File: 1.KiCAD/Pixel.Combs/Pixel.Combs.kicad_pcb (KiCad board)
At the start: 2 copper layers, 247 x 80 mm, 85 parts

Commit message: Updated Combs
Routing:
- net (no net): track 0.00 -> 328.9 mm, vias 57 -> 100

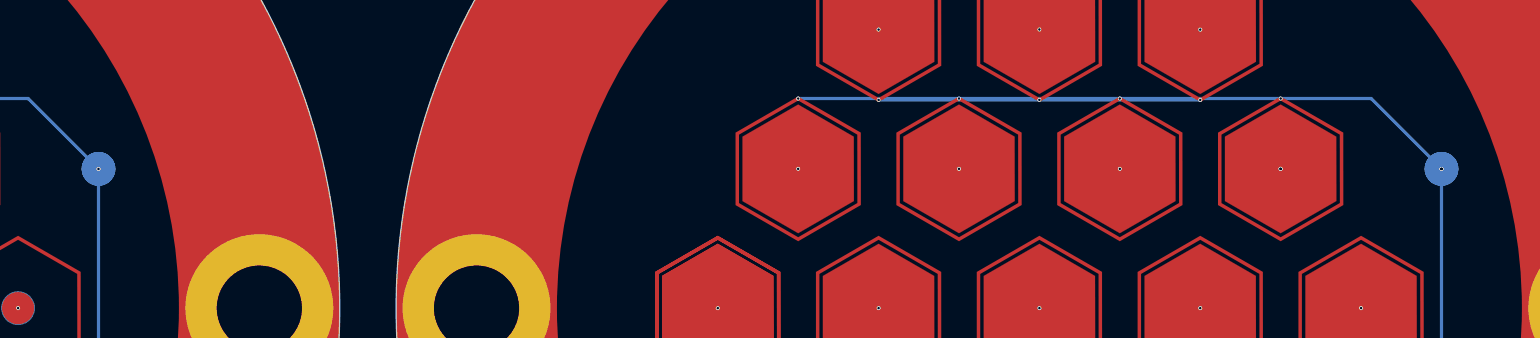
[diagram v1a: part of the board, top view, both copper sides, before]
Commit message: Spaced collection board traces
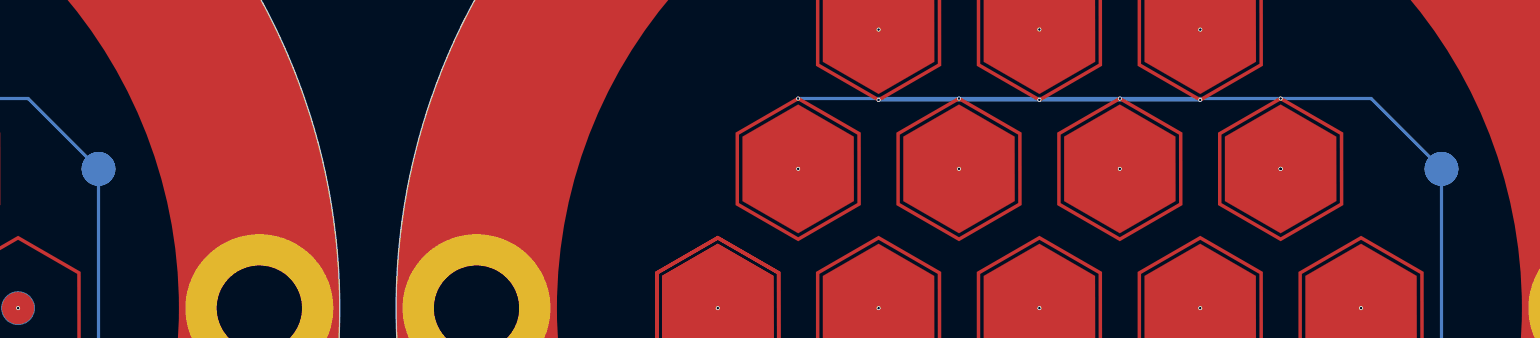
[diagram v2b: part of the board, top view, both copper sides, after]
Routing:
- net (no net): vias 100 -> 97
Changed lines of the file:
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@@
   (via blind (at 247.290237 56.129937) (size 0.25) (drill 0.15) (layers "F.Cu" "B.Cu") (net 0))
   (via blind (at 133.785 56.13) (size 0.25) (drill 0.15) (layers "F.Cu" "B.Cu") (net 0))
-  (via blind (at 257.290237 56.129937) (size 0.25) (drill 0.15) (layers "F.Cu" "B.Cu") (net 0))
   (via blind (at 138.785 82.11) (size 0.25) (drill 0.15) (layers "F.Cu" "B.Cu") (net 0))
   (via blind (at 158.785 77.735) (size 0.25) (drill 0.15) (layers "F.Cu" "B.Cu") (net 0))
@@
   (via blind (at 237.290237 56.129937) (size 0.25) (drill 0.15) (layers "F.Cu" "B.Cu") (net 0))
   (via blind (at 222.289859 64.790093) (size 0.25) (drill 0.15) (layers "F.Cu" "B.Cu") (net 0))
-  (via blind (at 173.785 56.13) (size 0.25) (drill 0.15) (layers "F.Cu" "B.Cu") (net 0))
   (via blind (at 138.785 69.165) (size 0.25) (drill 0.15) (layers "F.Cu" "B.Cu") (net 0))
   (via blind (at 60.280237 73.449937) (size 0.25) (drill 0.15) (layers "F.Cu" "B.Cu") (net 0))
@@
   (via blind (at 247.290237 69.074937) (size 0.25) (drill 0.15) (layers "F.Cu" "B.Cu") (net 0))
   (via blind (at 75.280237 64.789937) (size 0.25) (drill 0.15) (layers "F.Cu" "B.Cu") (net 0))
-  (via blind (at 257.290237 56.129937) (size 0.25) (drill 0.15) (layers "F.Cu" "B.Cu") (net 0))
   (via blind (at 153.785 73.45) (size 0.25) (drill 0.15) (layers "F.Cu" "B.Cu") (net 0))
   (via blind (at 50.280237 56.129937) (size 0.25) (drill 0.15) (layers "F.Cu" "B.Cu") (net 0))

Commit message: Thickened ground traces and updated channel wires
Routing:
- net (no net): track 328.9 -> 268.9 mm
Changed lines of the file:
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@@
   (via blind (at 217.289859 56.130093) (size 0.25) (drill 0.15) (layers "F.Cu" "B.Cu") (net 0))
   (via blind (at 70.280237 56.129937) (size 0.25) (drill 0.15) (layers "F.Cu" "B.Cu") (net 0))
-  (segment (start 169.41 51.755) (end 173.785 56.13) (width 0.2) (layer "B.Cu") (net 0))
+  (segment (start 169.41 51.755) (end 173.785 56.13) (width 1) (layer "B.Cu") (net 0))
   (segment (start 222.289859 51.845093) (end 242.290081 51.845093) (width 0.2) (layer "B.Cu") (net 0))
-  (segment (start 252.915237 51.754937) (end 257.290237 56.129937) (width 0.2) (layer "B.Cu") (net 0))
-  (segment (start 217.290237 69.074937) (end 247.290237 69.074937) (width 0.2) (layer "B.Cu") (net 0))
-  (segment (start 222.289859 69.165093) (end 222.289859 77.735093) (width 0.2) (layer "B.Cu") (net 0))
-  (segment (start 128.785 69.165) (end 168.785 69.165) (width 0.2) (layer "B.Cu") (net 0))
-  (segment (start 255.469907 69.165093) (end 252.289859 69.165093) (width 0.2) (layer "B.Cu") (net 0))
+  (segment (start 252.915237 51.754937) (end 257.290237 56.129937) (width 1) (layer "B.Cu") (net 0))
+  (segment (start 222.289859 69.165093) (end 222.289859 77.735093) (width 1) (layer "B.Cu") (net 0))
+  (segment (start 128.785 69.165) (end 168.785 69.165) (width 1) (layer "B.Cu") (net 0))
+  (segment (start 255.469907 69.165093) (end 252.289859 69.165093) (width 1) (layer "B.Cu") (net 0))
   (segment (start 242.290081 51.845093) (end 242.290237 51.844937) (width 0.2) (layer "B.Cu") (net 0))
-  (segment (start 257.290237 67.344763) (end 255.469907 69.165093) (width 0.2) (layer "B.Cu") (net 0))
-  (segment (start 173.785 56.13) (end 173.785 67.225) (width 0.2) (layer "B.Cu") (net 0))
-  (segment (start 217.289859 51.755093) (end 247.290081 51.755093) (width 0.2) (layer "B.Cu") (net 0))
-  (segment (start 133.785 51.755) (end 163.785 51.755) (width 0.2) (layer "B.Cu") (net 0))
-  (segment (start 247.290237 51.754937) (end 252.915237 51.754937) (width 0.2) (layer "B.Cu") (net 0))
-  (segment (start 133.785 69.075) (end 163.785 69.075) (width 0.2) (layer "B.Cu") (net 0))
-  (segment (start 158.785 77.735) (end 158.785 69.165) (width 0.2) (layer "B.Cu") (net 0))
-  (segment (start 212.289859 69.165093) (end 252.289859 69.165093) (width 0.2) (layer "B.Cu") (net 0))
-  (segment (start 242.289859 69.165093) (end 242.289859 77.735093) (width 0.2) (layer "B.Cu") (net 0))
-  (segment (start 148.785 77.735) (end 148.785 69.165) (width 0.2) (layer "B.Cu") (net 0))
-  (segment (start 173.785 67.225) (end 171.845 69.165) (width 0.2) (layer "B.Cu") (net 0))
-  (segment (start 163.785 51.755) (end 169.41 51.755) (width 0.2) (layer "B.Cu") (net 0))
+  (segment (start 257.290237 67.344763) (end 255.469907 69.165093) (width 1) (layer "B.Cu") (net 0))
+  (segment (start 173.785 56.13) (end 173.785 67.225) (width 1) (layer "B.Cu") (net 0))
+  (segment (start 217.289859 51.755093) (end 247.290081 51.755093) (width 1) (layer "B.Cu") (net 0))
+  (segment (start 133.785 51.755) (end 163.785 51.755) (width 1) (layer "B.Cu") (net 0))
+  (segment (start 247.290237 51.754937) (end 252.915237 51.754937) (width 1) (layer "B.Cu") (net 0))
+  (segment (start 158.785 77.735) (end 158.785 69.165) (width 1) (layer "B.Cu") (net 0))
+  (segment (start 212.289859 69.165093) (end 252.289859 69.165093) (width 1) (layer "B.Cu") (net 0))
+  (segment (start 242.289859 69.165093) (end 242.289859 77.735093) (width 1) (layer "B.Cu") (net 0))
+  (segment (start 148.785 77.735) (end 148.785 69.165) (width 1) (layer "B.Cu") (net 0))
+  (segment (start 173.785 67.225) (end 171.845 69.165) (width 1) (layer "B.Cu") (net 0))
+  (segment (start 163.785 51.755) (end 169.41 51.755) (width 1) (layer "B.Cu") (net 0))
   (segment (start 247.290081 51.755093) (end 247.290237 51.754937) (width 0.2) (layer "B.Cu") (net 0))
-  (segment (start 232.290237 77.734937) (end 232.290237 69.164937) (width 0.2) (layer "B.Cu") (net 0))
-  (segment (start 171.845 69.165) (end 168.785 69.165) (width 0.2) (layer "B.Cu") (net 0))
-  (segment (start 257.290237 56.129937) (end 257.290237 67.344763) (width 0.2) (layer "B.Cu") (net 0))
-  (segment (start 138.785 77.735) (end 138.785 69.165) (width 0.2) (layer "B.Cu") (net 0))
+  (segment (start 232.290237 77.734937) (end 232.290237 69.164937) (width 1) (layer "B.Cu") (net 0))
+  (segment (start 171.845 69.165) (end 168.785 69.165) (width 1) (layer "B.Cu") (net 0))
+  (segment (start 257.290237 56.129937) (end 257.290237 67.344763) (width 1) (layer "B.Cu") (net 0))
+  (segment (start 138.785 77.735) (end 138.785 69.165) (width 1) (layer "B.Cu") (net 0))
 )

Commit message: A
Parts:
- added ?: , , F.Cu at (100.0, 148.3)
- added ?: , , F.Cu at (65.0, 113.3)
- added ?: , , F.Cu at (173.2, 173.0)
- added ?: , , F.Cu at (256.7, 173.0)
- added ?: , , F.Cu at (89.7, 123.5)
- added ?: , , F.Cu at (123.7, 173.0)
- added ?: , , F.Cu at (183.5, 148.3)
- added ?: , , F.Cu at (40.2, 123.5)
- added ?: , , F.Cu at (123.7, 123.5)
- added ?: , , F.Cu at (148.5, 183.3)
- added ?: , , F.Cu at (173.2, 123.5)
- added ?: , , F.Cu at (207.2, 123.5)
- added ?: , , F.Cu at (267.0, 148.3)
- added ?: , , F.Cu at (232.0, 113.3)
- added ?: , , F.Cu at (148.5, 113.3)
- added ?: , , F.Cu at (113.5, 148.3)
- added ?: , , F.Cu at (197.0, 148.3)
- added ?: , , F.Cu at (207.2, 173.0)
- added ?: , , F.Cu at (89.7, 173.0)
- added ?: , , F.Cu at (40.2, 173.0)
- added ?: , , F.Cu at (30.0, 148.3)
- added ?: , , F.Cu at (65.0, 183.3)
- added ?: , , F.Cu at (256.7, 123.5)
- added ?: , , F.Cu at (232.0, 183.3)
- added G***: LOGO, LOGO, B.Cu at (219.6, 178.2)
- added G***: Designed by Alfredo Barajas Enriquez, LOGO, B.Cu at (52.6, 178.2)
- added G***: LOGO, LOGO, B.Cu at (136.1, 178.2)
- added REF**: Hex.Tile.Solid.Hex, Hex:Hex.Tile.Solid.Hex, F.Cu at (65.0, 148.3)
- added REF**: Hex.Tile.Solid.G.Hex, 1.Hex:Hex.Tile.Solid.G.Hex, F.Cu at (232.0, 148.3)
- added REF**: Hex.Tile.Solid.G.Dot, Hex:Hex.Tile.Solid.G.Dot, F.Cu at (148.5, 148.3)
- added REF**1: Hex.Tile.Solid.Hex, Hex:Hex.Tile.Solid.Hex, F.Cu at (75.0, 148.3)
- added REF**10: Hex.Tile.Solid.G.Dot, Hex:Hex.Tile.Solid.G.Dot, F.Cu at (153.5, 139.6)
- added REF**11: Hex.Tile.Solid.G.Dot, Hex:Hex.Tile.Solid.G.Dot, F.Cu at (163.5, 139.6)
- added REF**12: Hex.Tile.Solid.G.Hex, 1.Hex:Hex.Tile.Solid.G.Hex, F.Cu at (252.0, 148.3)
- added REF**13: Hex.Tile.Solid.G.Dot, Hex:Hex.Tile.Solid.G.Dot, F.Cu at (138.5, 131.0)
- added REF**14: Hex.Tile.Solid.G.Dot, Hex:Hex.Tile.Solid.G.Dot, F.Cu at (148.5, 131.0)
- added REF**15: Hex.Tile.Solid.G.Dot, Hex:Hex.Tile.Solid.G.Dot, F.Cu at (158.5, 131.0)
- added REF**18: Hex.Tile.Solid.G.Hex, 1.Hex:Hex.Tile.Solid.G.Hex, F.Cu at (237.0, 157.0)
- added REF**19: Hex.Tile.Solid.Hex, Hex:Hex.Tile.Solid.Hex, F.Cu at (60.0, 139.6)
- added REF**2: Hex.Tile.Solid.Hex, Hex:Hex.Tile.Solid.Hex, F.Cu at (85.0, 148.3)
- added REF**20: Hex.Tile.Solid.Hex, Hex:Hex.Tile.Solid.Hex, F.Cu at (70.0, 139.6)
- added REF**21: Hex.Tile.Solid.Hex, Hex:Hex.Tile.Solid.Hex, F.Cu at (80.0, 139.6)
- added REF**22: Hex.Tile.Solid.G.Hex, 1.Hex:Hex.Tile.Solid.G.Hex, F.Cu at (247.0, 157.0)
- added REF**23: Hex.Tile.Solid.Hex, Hex:Hex.Tile.Solid.Hex, F.Cu at (55.0, 131.0)
- added REF**24: Hex.Tile.Solid.Hex, Hex:Hex.Tile.Solid.Hex, F.Cu at (65.0, 131.0)
- added REF**25: Hex.Tile.Solid.Hex, Hex:Hex.Tile.Solid.Hex, F.Cu at (75.0, 131.0)
- added REF**29: Hex.Tile.Solid.G.Hex, 1.Hex:Hex.Tile.Solid.G.Hex, F.Cu at (242.0, 165.6)
- added REF**3: Hex.Tile.Solid.G.Dot, Hex:Hex.Tile.Solid.G.Dot, F.Cu at (158.5, 148.3)
- added REF**30: Hex.Tile.Solid.G.Dot, Hex:Hex.Tile.Solid.G.Dot, F.Cu at (153.5, 157.0)
- added REF**31: Hex.Tile.Solid.Hex, Hex:Hex.Tile.Solid.Hex, F.Cu at (55.0, 148.3)
- added REF**32: Hex.Tile.Solid.Hex, Hex:Hex.Tile.Solid.Hex, F.Cu at (45.0, 148.3)
- added REF**33: Hex.Tile.Solid.G.Dot, Hex:Hex.Tile.Solid.G.Dot, F.Cu at (163.5, 157.0)
- added REF**35: Hex.Tile.Solid.Hex, Hex:Hex.Tile.Solid.Hex, F.Cu at (60.0, 157.0)
- added REF**36: Hex.Tile.Solid.Hex, Hex:Hex.Tile.Solid.Hex, F.Cu at (50.0, 157.0)
- added REF**38: Hex.Tile.Solid.G.Dot, Hex:Hex.Tile.Solid.G.Dot, F.Cu at (158.5, 165.6)
- added REF**39: Hex.Tile.Solid.Hex, Hex:Hex.Tile.Solid.Hex, F.Cu at (65.0, 165.6)
- added REF**4: Hex.Tile.Solid.Hex, Hex:Hex.Tile.Solid.Hex, F.Cu at (70.0, 157.0)
- added REF**40: Hex.Tile.Solid.Hex, Hex:Hex.Tile.Solid.Hex, F.Cu at (55.0, 165.6)
- added REF**49: Hex.Tile.Solid.Hex, Hex:Hex.Tile.Solid.Hex, F.Cu at (50.0, 139.6)
- added REF**5: Hex.Tile.Solid.Hex, Hex:Hex.Tile.Solid.Hex, F.Cu at (80.0, 157.0)
- added REF**50: Hex.Tile.Solid.G.Dot, Hex:Hex.Tile.Solid.G.Dot, F.Cu at (128.5, 148.3)
- added REF**53: Hex.Tile.Solid.G.Dot, Hex:Hex.Tile.Solid.G.Dot, F.Cu at (133.5, 139.6)
- added REF**59: Hex.Tile.Solid.G.Hex, 1.Hex:Hex.Tile.Solid.G.Hex, F.Cu at (227.0, 139.6)
- added REF**6: Hex.Tile.Solid.G.Dot, Hex:Hex.Tile.Solid.G.Dot, F.Cu at (168.5, 148.3)
- added REF**60: Hex.Tile.Solid.G.Hex, 1.Hex:Hex.Tile.Solid.G.Hex, F.Cu at (237.0, 139.6)
- added REF**61: Hex.Tile.Solid.G.Hex, 1.Hex:Hex.Tile.Solid.G.Hex, F.Cu at (247.0, 139.6)
- added REF**63: Hex.Tile.Solid.G.Hex, 1.Hex:Hex.Tile.Solid.G.Hex, F.Cu at (222.0, 131.0)
- added REF**64: Hex.Tile.Solid.G.Dot, Hex:Hex.Tile.Solid.G.Dot, F.Cu at (138.5, 148.3)
- added REF**65: Hex.Tile.Solid.G.Hex, 1.Hex:Hex.Tile.Solid.G.Hex, F.Cu at (232.0, 131.0)
- added REF**66: Hex.Tile.Solid.G.Hex, 1.Hex:Hex.Tile.Solid.G.Hex, F.Cu at (242.0, 131.0)
- added REF**67: Hex.Tile.Solid.G.Dot, Hex:Hex.Tile.Solid.G.Dot, F.Cu at (143.5, 157.0)
- added REF**68: Hex.Tile.Solid.G.Dot, Hex:Hex.Tile.Solid.G.Dot, F.Cu at (133.5, 157.0)
- added REF**7: Hex.Tile.Solid.G.Hex, 1.Hex:Hex.Tile.Solid.G.Hex, F.Cu at (242.0, 148.3)
- added REF**71: Hex.Tile.Solid.G.Dot, Hex:Hex.Tile.Solid.G.Dot, F.Cu at (138.5, 165.6)
- added REF**75: Hex.Tile.Solid.G.Hex, 1.Hex:Hex.Tile.Solid.G.Hex, F.Cu at (222.0, 148.3)
- added REF**76, REF**91: Hex.Tile.Solid.G.Hex, 1.Hex:Hex.Tile.Solid.G.Hex, F.Cu at (212.0, 148.3)
- added REF**79: Hex.Tile.Solid.G.Hex, 1.Hex:Hex.Tile.Solid.G.Hex, F.Cu at (227.0, 157.0)
- added REF**8: Hex.Tile.Solid.Hex, Hex:Hex.Tile.Solid.Hex, F.Cu at (75.0, 165.6)
- added REF**80: Hex.Tile.Solid.G.Dot, Hex:Hex.Tile.Solid.G.Dot, F.Cu at (148.5, 165.6)
- added REF**81: Hex.Tile.Solid.G.Hex, 1.Hex:Hex.Tile.Solid.G.Hex, F.Cu at (217.0, 157.0)
- added REF**84: Hex.Tile.Solid.G.Hex, 1.Hex:Hex.Tile.Solid.G.Hex, F.Cu at (232.0, 165.6)
- added REF**85: Hex.Tile.Solid.G.Hex, 1.Hex:Hex.Tile.Solid.G.Hex, F.Cu at (222.0, 165.6)
- added REF**9: Hex.Tile.Solid.G.Dot, Hex:Hex.Tile.Solid.G.Dot, F.Cu at (143.5, 139.6)
- added REF**94: Hex.Tile.Solid.G.Hex, 1.Hex:Hex.Tile.Solid.G.Hex, F.Cu at (217.0, 139.6)
- moved ? 6.50 mm to (207.2, 83.0)
- moved G*** 6.50 mm to (219.6, 88.2)
- moved REF**29 6.50 mm to (242.0, 75.6)
- moved REF**84 6.50 mm to (232.0, 75.6)
- moved REF**85 6.50 mm to (222.0, 75.6)
- moved ? 6.50 mm to (123.7, 83.0)
- moved ? 6.50 mm to (89.7, 83.0)
- moved ? 6.50 mm to (173.2, 83.0)
- moved ? 6.50 mm to (40.2, 83.0)
- moved REF** 6.50 mm to (148.5, 58.3)
- moved REF**3 6.50 mm to (158.5, 58.3)
- moved REF**30 6.50 mm to (153.5, 67.0)
- moved REF**33 6.50 mm to (163.5, 67.0)
- moved REF**35 6.50 mm to (60.0, 67.0)
- moved REF**36 6.50 mm to (50.0, 67.0)
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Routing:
- net (no net): track 268.9 -> 537.8 mm, vias 97 -> 194
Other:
- board size 247 x 80 mm -> 247 x 170 mm
